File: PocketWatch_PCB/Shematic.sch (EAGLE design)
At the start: 44 parts, among them U2 ATTINY88-AU

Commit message: Added Dimensions
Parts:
- removed T1, T2, T3, T4: (no value), transistor:MMBT918LT1-NPN-SOT23-BEC
- added IC1: 74HC139D, 74xx-eu:74HC139D
- added Q1, Q2, Q3, Q4: BCX71SMD, transistor-pnp:BCX71SMD
- added Q5, Q6, Q7, Q8: BCX70SMD, transistor-npn:BCX70SMD
- added SV4: (no value), con-lstb:MA05-1
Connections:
- net TG0_2 renamed T0_2
- net TG1_2 renamed T1_2
- net TG2_2 renamed T2_2
- net TG3_2 renamed T3_2
- removed net EN0: R5.1, U2.PA0_(ADC6/PCINT24)
- removed net EN1: R6.1, U2.PA1_(ADC7/PCINT25)
- removed net EN2: R7.1, U2.PA2_(PCINT26)
- removed net EN3: R8.1, U2.PA3_(PCINT27)
- removed net TG0: SV5.4, T1.C
- removed net TG1: SV5.3, T2.C
- removed net TG2: SV5.2, T3.C
- removed net TG3: SV5.1, T4.C
- new net HEF: U2.PC7_(PCINT15)
- new net M0: Q5.B, U2.PA0_(ADC6/PCINT24)
- new net M1: Q6.B, U2.PA1_(ADC7/PCINT25)
- new net M2: Q7.B, U2.PA2_(PCINT26)
- new net M3: Q8.B, U2.PA3_(PCINT27)
- new net N$10: IC1A.Y1, R6.1
- new net N$11: IC1A.Y2, R7.1
- new net N$13: IC1A.Y3, R8.1
- new net N$18: IC1B.Y3, R14.2
- new net N$19: Q5.C, SV4.1
- new net N$20: Q6.C, SV4.2
- new net N$21: Q7.C, SV4.3
- new net N$22: Q8.C, SV4.4
- new net N$27: IC1B.B, U2.PB6_(PCINT6/CLKI)
- new net N$28: IC1B.A, U2.PB7_(PCINT7)
- new net N$8: IC1A.Y0, R5.1
- new net T0: Q1.C, SV5.4
- new net T1: Q2.C, SV5.3
- new net T2: Q3.C, SV5.2
- new net T3: Q4.C, SV5.1
- new net TC0: IC1A.A, U2.PB0_(PCINT0/CLKO/ICP1)
- new net TC1: IC1A.B, U2.PB1_(PCINT1/OC1A)
- net GND: now also IC1A.G, IC1B.G, Q5.E, Q6.E, Q7.E, Q8.E; no longer AM.C, COLIN1.C, COLIN2.C, PM.C, T1.E, T2.E, T3.E, T4.E
- net N$1: now also Q4.B; no longer T4.B
- net N$15: now also IC1B.Y0, R17.2; no longer R14.2, R15.2, U2.PB0_(PCINT0/CLKO/ICP1)
- net N$16: now also IC1B.Y1, R16.2; no longer R17.2, U2.PB2_(PCINT2/!SS!/OC1B)
- net N$17: now also IC1B.Y2, R15.2; no longer R16.2, U2.PB1_(PCINT1/OC1A)
- net N$2: now also Q3.B; no longer T3.B
- net N$3: now also Q2.B; no longer T2.B
- net N$5: now also Q1.B; no longer T1.B
- net VCC: now also AM.C, COLIN1.C, COLIN2.C, PM.C, Q1.E, Q2.E, Q3.E, Q4.E, SV4.5
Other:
- moved on the sheet: AM, B_DOWN, B_SEL, B_UP, COLIN1, COLIN2, PM, R14, R15, R16, R17, R18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

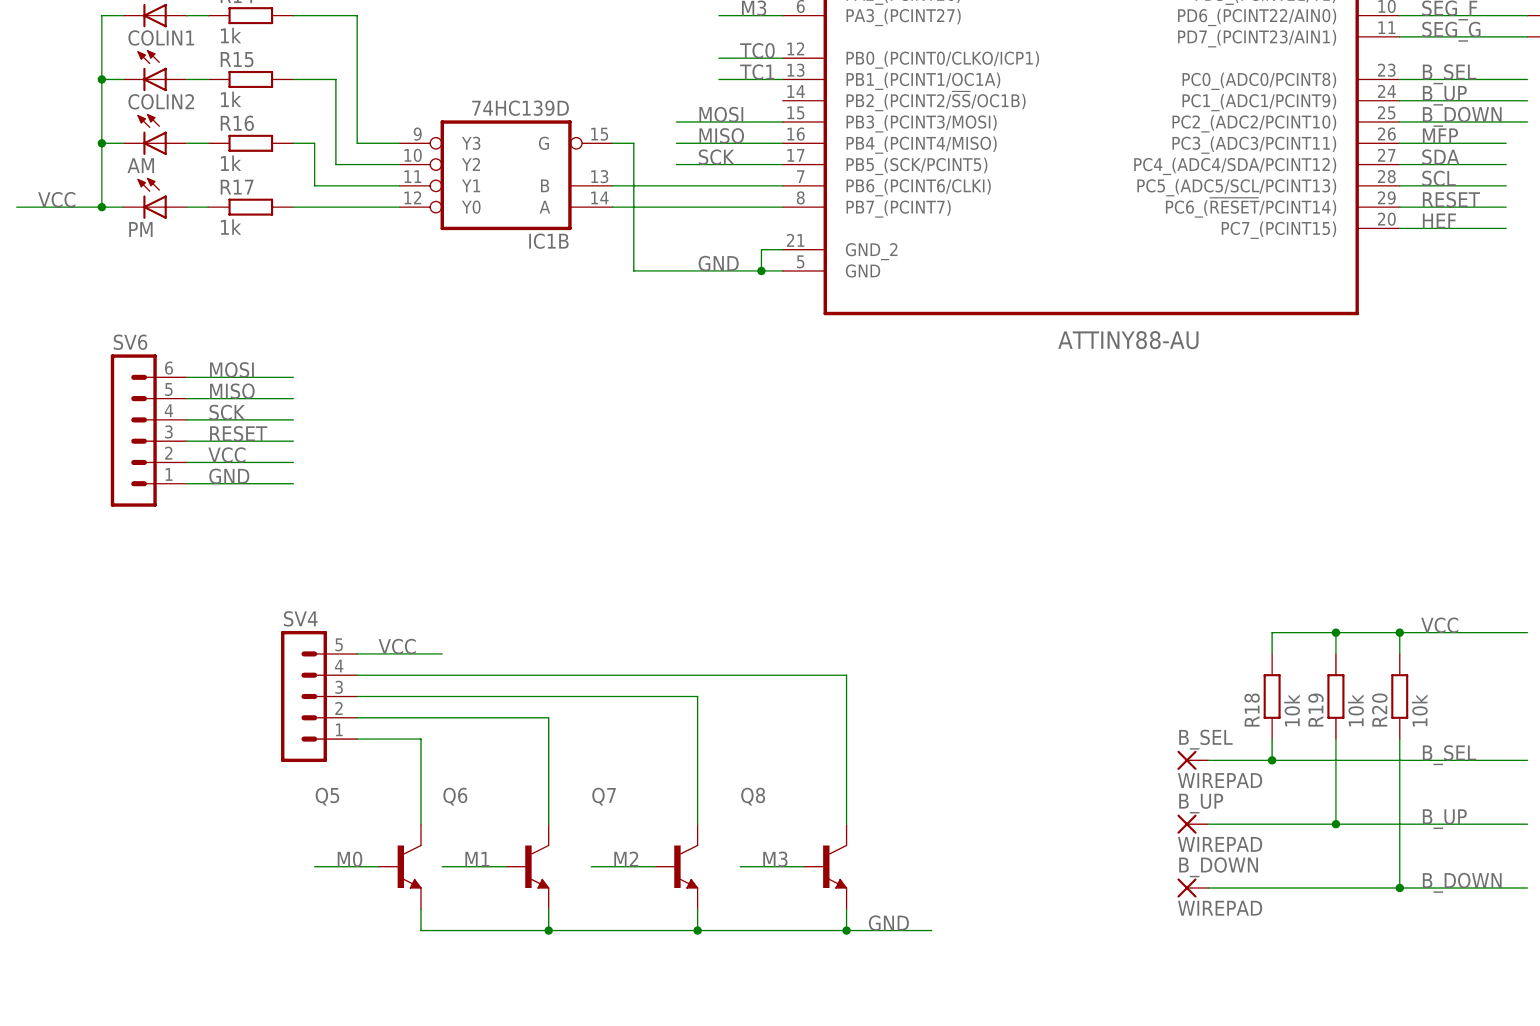
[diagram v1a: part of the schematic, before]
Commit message: Completed most of the routing
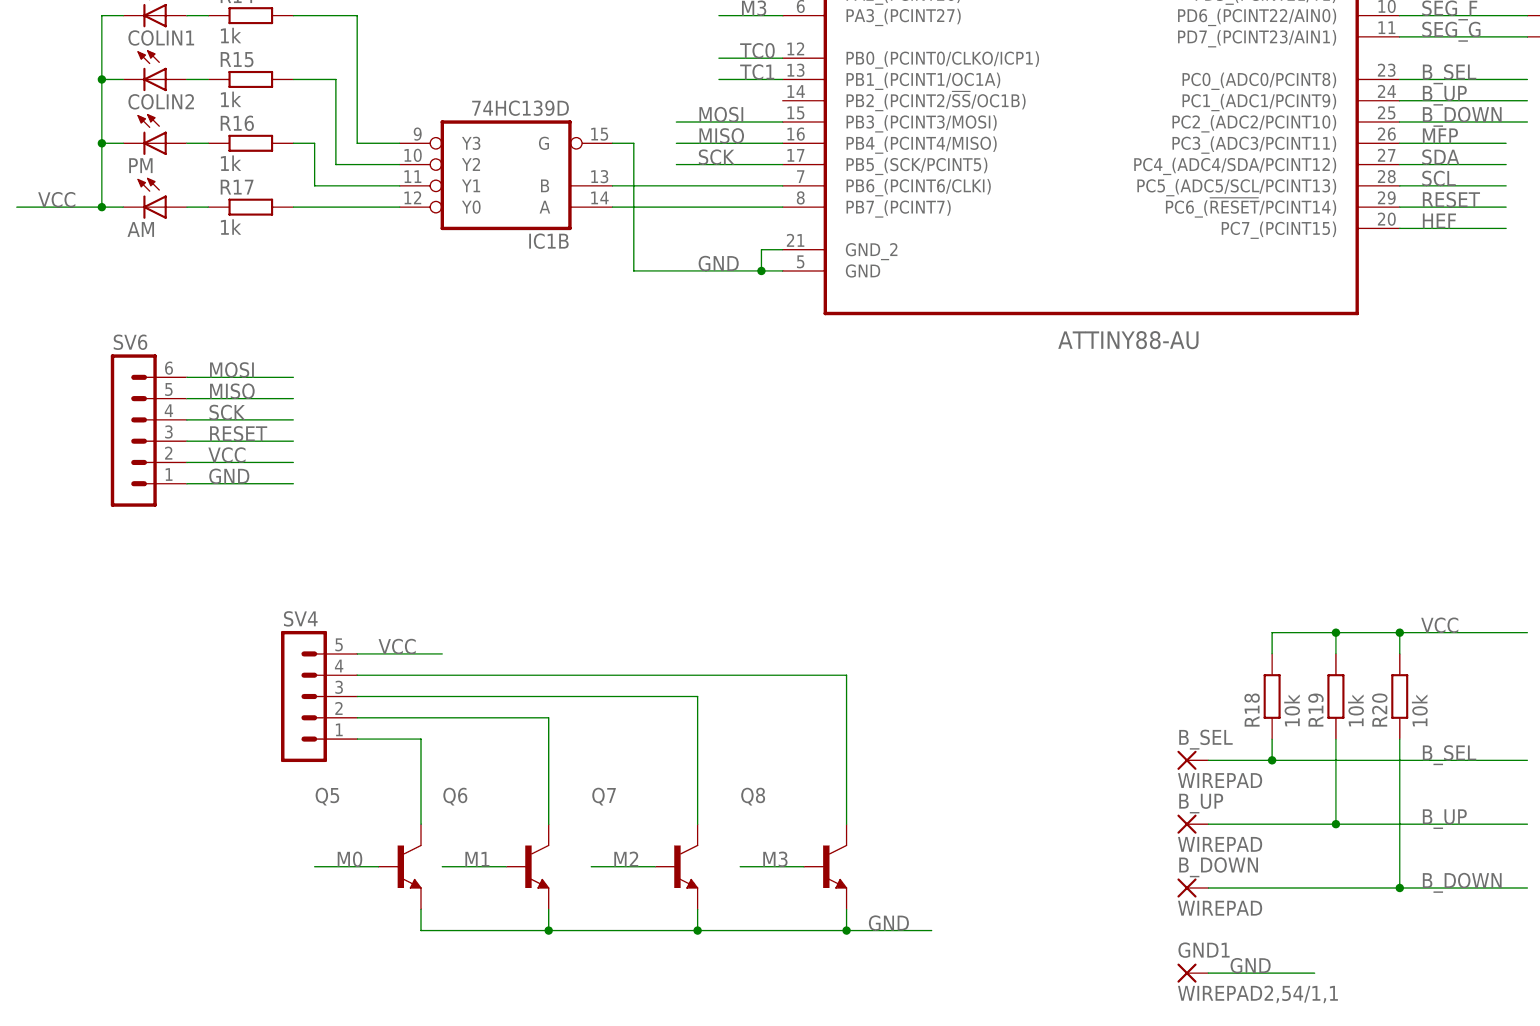
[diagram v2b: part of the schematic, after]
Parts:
- added GND1: WIREPAD2,54/1,1, wirepad:WIREPAD2,54/1,1
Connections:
- net GND: now also GND1.P
- net N$12: now also PM.A; no longer AM.A
- net N$14: now also AM.A; no longer PM.A
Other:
- moved on the sheet: AM, PM
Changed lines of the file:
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@@
 <part name="Q7" library="transistor-npn" library_urn="urn:adsk.eagle:library:398" deviceset="BCX70*" device="SMD" package3d_urn="urn:adsk.eagle:package:28984/2" value=""/>
 <part name="Q8" library="transistor-npn" library_urn="urn:adsk.eagle:library:398" deviceset="BCX70*" device="SMD" package3d_urn="urn:adsk.eagle:package:28984/2" value=""/>
+<part name="GND1" library="wirepad" library_urn="urn:adsk.eagle:library:412" deviceset="WIREPAD" device="2,54/1,1" package3d_urn="urn:adsk.eagle:package:30836/1"/>
 </parts>
 <sheets>
@@
 <instance part="B_UP" gate="G$1" x="76.2" y="-93.98"/>
 <instance part="B_DOWN" gate="G$1" x="76.2" y="-101.6"/>
-<instance part="AM" gate="G$1" x="-45.72" y="-12.7" rot="R270"/>
-<instance part="PM" gate="G$1" x="-45.72" y="-20.32" rot="R270"/>
+<instance part="AM" gate="G$1" x="-45.72" y="-20.32" rot="R270"/>
+<instance part="PM" gate="G$1" x="-45.72" y="-12.7" rot="R270"/>
 <instance part="COLIN1" gate="G$1" x="-45.72" y="2.54" rot="R270"/>
 <instance part="R14" gate="G$1" x="-35.56" y="2.54"/>
@@
 <instance part="Q7" gate="G$1" x="15.24" y="-99.06"/>
 <instance part="Q8" gate="G$1" x="33.02" y="-99.06"/>
+<instance part="GND1" gate="G$1" x="76.2" y="-111.76"/>
 </instances>
 <busses>
@@
 <label x="38.1" y="-106.68" size="1.778" layer="95"/>
 </segment>
+<segment>
+<wire x1="78.74" y1="-111.76" x2="91.44" y2="-111.76" width="0.1524" layer="91"/>
+<label x="81.28" y="-111.76" size="1.778" layer="95"/>
+<pinref part="GND1" gate="G$1" pin="P"/>
+</segment>
 </net>
 <net name="VCC" class="0">
@@
 <wire x1="-53.34" y1="-12.7" x2="-53.34" y2="-20.32" width="0.1524" layer="91"/>
 <wire x1="-53.34" y1="-20.32" x2="-63.5" y2="-20.32" width="0.1524" layer="91"/>
-<pinref part="PM" gate="G$1" pin="C"/>
-<wire x1="-50.8" y1="-20.32" x2="-53.34" y2="-20.32" width="0.1524" layer="91"/>
-<junction x="-53.34" y="-20.32"/>
-<pinref part="AM" gate="G$1" pin="C"/>
-<wire x1="-50.8" y1="-12.7" x2="-53.34" y2="-12.7" width="0.1524" layer="91"/>
-<junction x="-53.34" y="-12.7"/>
 <pinref part="COLIN2" gate="G$1" pin="C"/>
 <wire x1="-50.8" y1="-5.08" x2="-53.34" y2="-5.08" width="0.1524" layer="91"/>
 <junction x="-53.34" y="-5.08"/>
 <label x="-60.96" y="-20.32" size="1.778" layer="95"/>
+<pinref part="AM" gate="G$1" pin="C"/>
+<wire x1="-50.8" y1="-20.32" x2="-53.34" y2="-20.32" width="0.1524" layer="91"/>
+<junction x="-53.34" y="-20.32"/>
+<pinref part="PM" gate="G$1" pin="C"/>
+<wire x1="-50.8" y1="-12.7" x2="-53.34" y2="-12.7" width="0.1524" layer="91"/>
+<junction x="-53.34" y="-12.7"/>
 </segment>
 <segment>
@@
 </segment>
 </net>
-<net name="N$12" class="0">
-<segment>
-<pinref part="R16" gate="G$1" pin="1"/>
-<pinref part="AM" gate="G$1" pin="A"/>
-<wire x1="-40.64" y1="-12.7" x2="-43.18" y2="-12.7" width="0.1524" layer="91"/>
-</segment>
-</net>
-<net name="N$14" class="0">
-<segment>
-<pinref part="R17" gate="G$1" pin="1"/>
-<pinref part="PM" gate="G$1" pin="A"/>
-<wire x1="-40.64" y1="-20.32" x2="-43.18" y2="-20.32" width="0.1524" layer="91"/>
-</segment>
-</net>
 <net name="TGND" class="0">
 <segment>
@@
 </segment>
 </net>
+<net name="N$12" class="0">
+<segment>
+<pinref part="R16" gate="G$1" pin="1"/>
+<pinref part="PM" gate="G$1" pin="A"/>
+<wire x1="-40.64" y1="-12.7" x2="-43.18" y2="-12.7" width="0.1524" layer="91"/>
+</segment>
+</net>
+<net name="N$14" class="0">
+<segment>
+<pinref part="R17" gate="G$1" pin="1"/>
+<pinref part="AM" gate="G$1" pin="A"/>
+<wire x1="-40.64" y1="-20.32" x2="-43.18" y2="-20.32" width="0.1524" layer="91"/>
+</segment>
+</net>

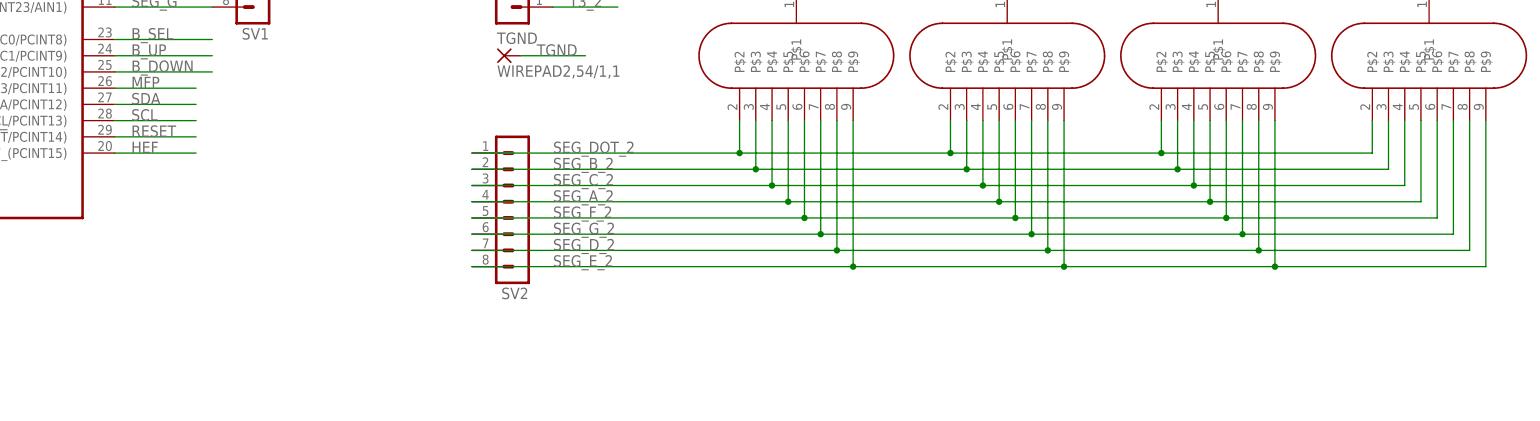
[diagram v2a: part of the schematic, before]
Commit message: Completed PCB layout. Passes DRC.
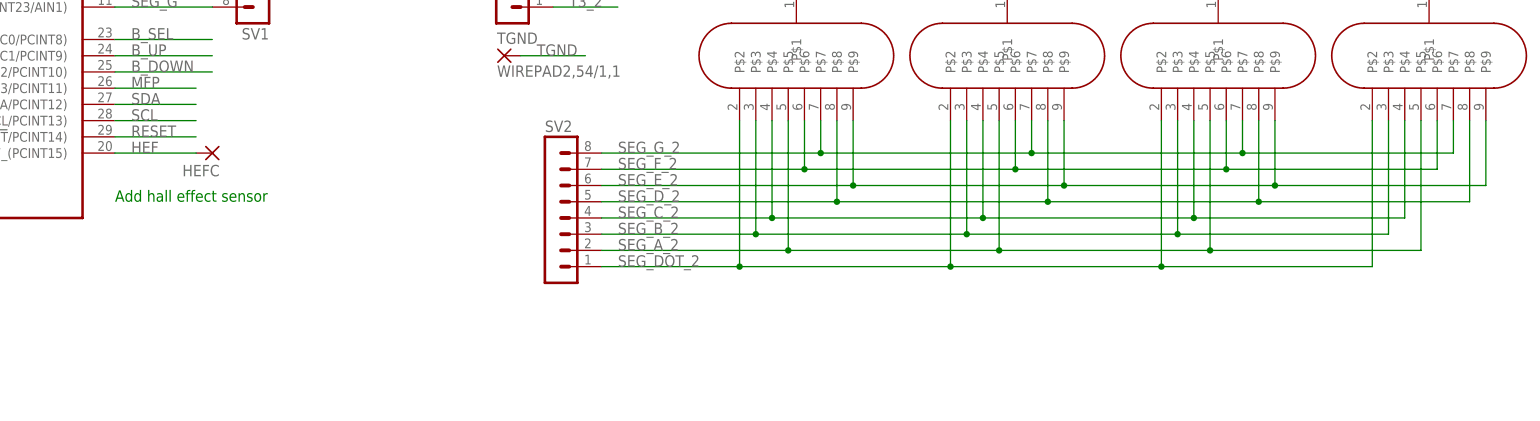
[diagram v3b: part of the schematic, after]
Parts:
- added HEFC: WIREPAD2,54/1,1, wirepad:WIREPAD2,54/1,1
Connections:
- net HEF: now also HEFC.P
- net SEG_A_2: now also SV2.2; no longer SV2.4
- net SEG_B_2: now also SV2.3; no longer SV2.2
- net SEG_C_2: now also SV2.4; no longer SV2.3
- net SEG_D_2: now also SV2.5; no longer SV2.7
- net SEG_E_2: now also SV2.6; no longer SV2.8
- net SEG_F_2: now also SV2.7; no longer SV2.5
- net SEG_G_2: now also SV2.8; no longer SV2.6
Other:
- note added: "Add hall effect sensor"
- moved on the sheet: SV2

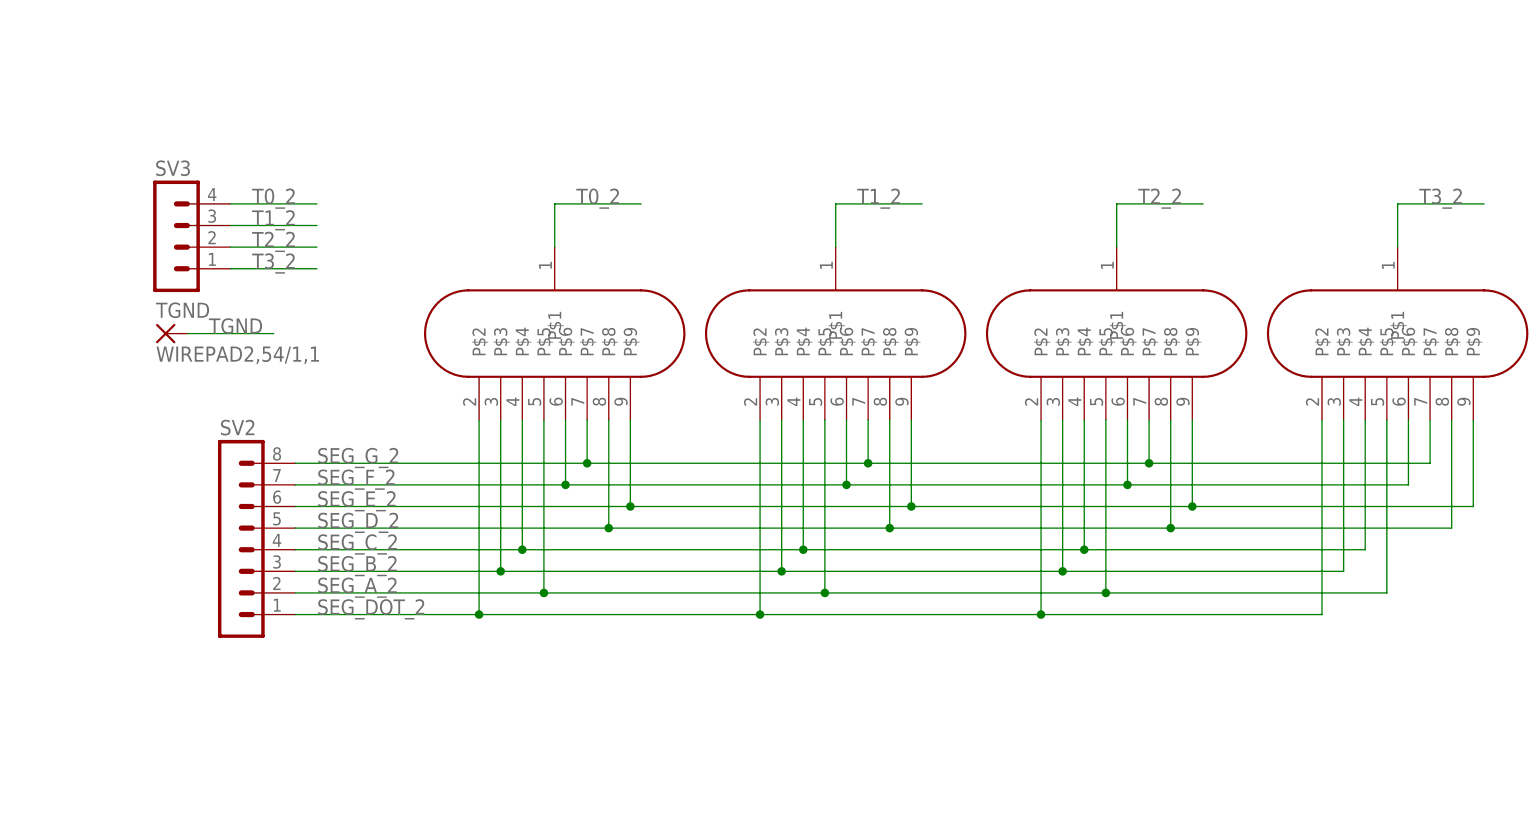
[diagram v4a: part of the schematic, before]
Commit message: Rearranged bottom board to be much more thin.
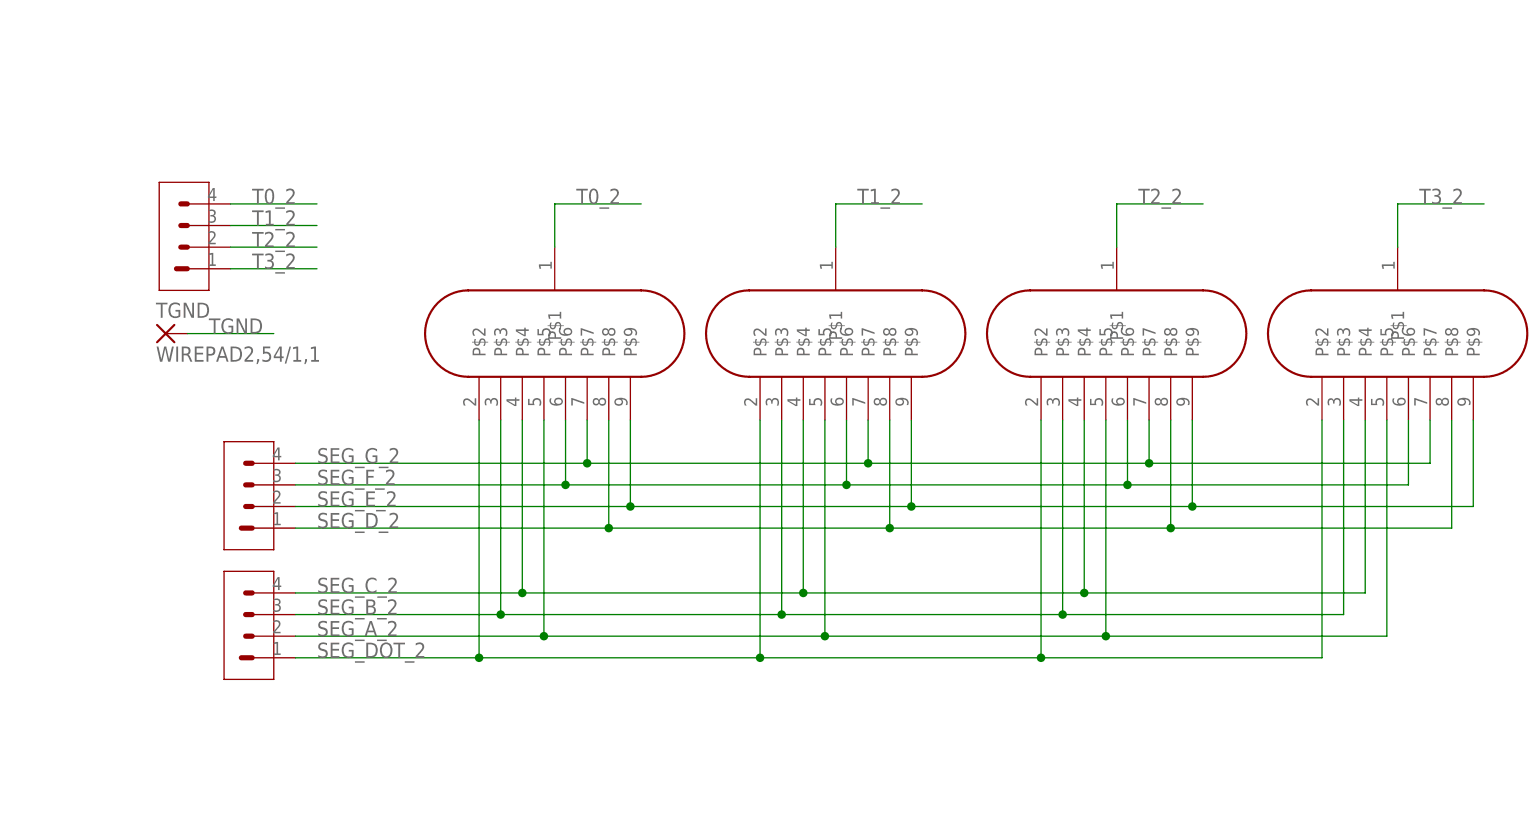
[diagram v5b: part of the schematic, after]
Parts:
- added SV7: H04, Library:H04
- SV2: value (none) -> H04; device con-lstb:MA08-1 -> Library:H04
- SV3: value (none) -> H04; device con-lstb:MA04-1 -> Library:H04
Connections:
- net SEG_A_2: now also SV7.2; no longer SV2.2
- net SEG_B_2: now also SV7.3; no longer SV2.3
- net SEG_C_2: now also SV7.4; no longer SV2.4
- net SEG_DOT_2: now also SV7.1; no longer SV2.1
- net SEG_D_2: now also SV2.1; no longer SV2.5
- net SEG_E_2: now also SV2.2; no longer SV2.6
- net SEG_F_2: now also SV2.3; no longer SV2.7
- net SEG_G_2: now also SV2.4; no longer SV2.8
